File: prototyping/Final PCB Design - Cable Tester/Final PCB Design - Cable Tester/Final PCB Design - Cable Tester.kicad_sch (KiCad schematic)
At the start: 41 parts, among them J17 Banana Jack, J20 SFML-110-02-L-D-A, J3 Debug Connection, J4 MEM2061-01-188-00-A_REVA, J5 Barrel Jack 9V, J6 Touchscreen HMI, Q1 2N3904, SW1 Rocker Switch, U1 AVR128DB64x-xMR, U2 LP2985-3.3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

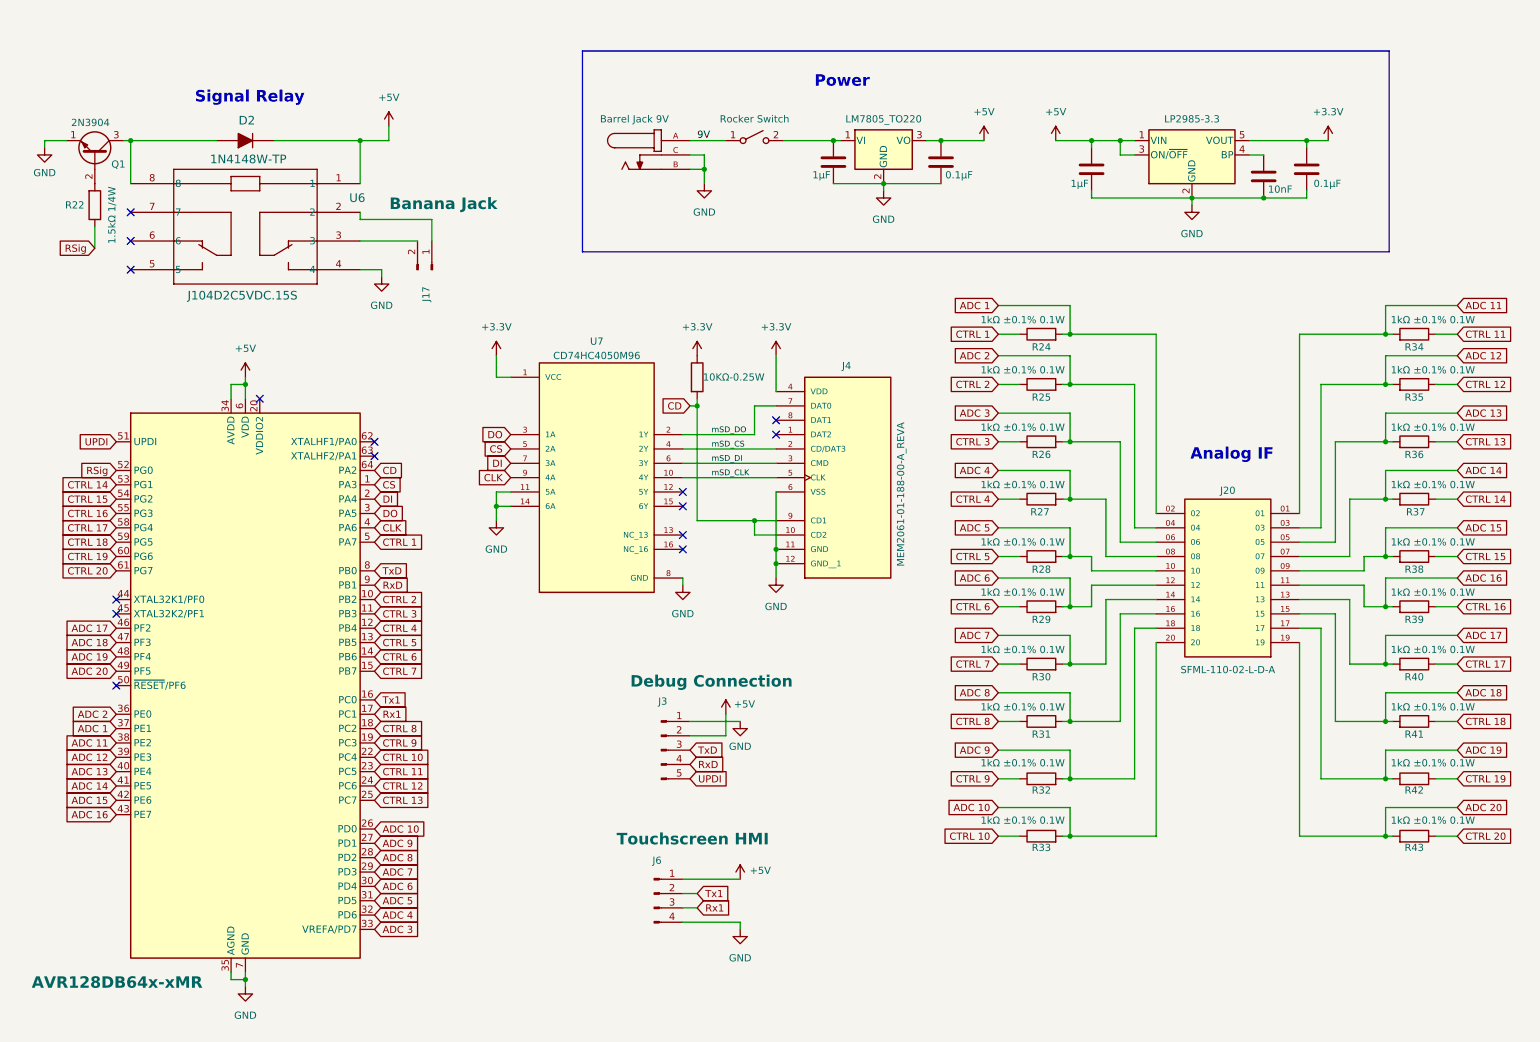
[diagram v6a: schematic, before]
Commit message: Update - Final PCB to JLCPCB components
Added the JLCPCB Library and updated to equivalent components supplied by JLCPCB. Also updated the PCB traces to fit new components.
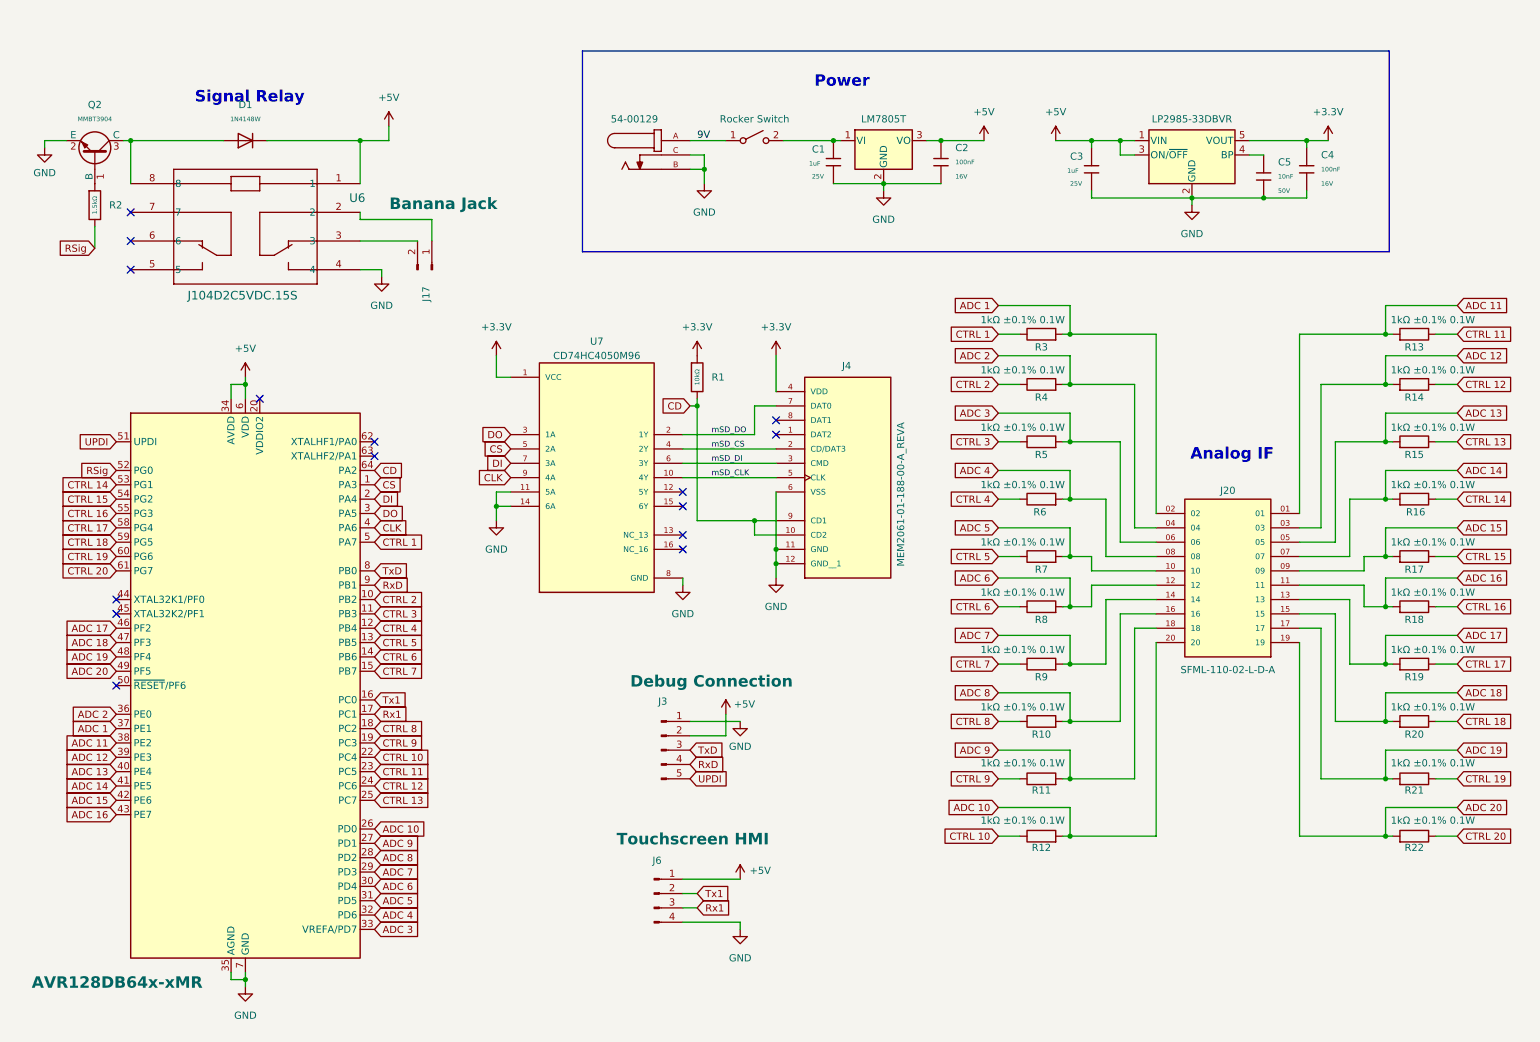
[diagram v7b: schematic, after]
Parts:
- removed C1, C3: 1µF, KiCad Symbols and Footprints:CAP_CL10_SAM, symbol Device:C
- removed C2, C4: 0.1µF, KiCad Symbols and Footprints:CAP_CL05_SAM, symbol Device:C
- removed C5: 10nF, KiCad Symbols and Footprints:CAPC10555_55N_KEM, symbol Device:C
- removed D2: 1N4148W-TP, digikey-footprints:SOD-123, symbol dk_Diodes-Rectifiers-Single:1N4148W-TP
- removed Q1: 2N3904, Package_TO_SOT_THT:TO-92_Inline, symbol Transistor_BJT:2N3904
- removed R2: 10KΩ-0.25W, KiCad Symbols and Footprints:RC0402N_PAN, symbol Device:R
- removed R22: 1.5kΩ 1/4W, KiCad Symbols and Footprints:RES_ERA8AEB152V, symbol Device:R
- added C1, C3: 1uF, PCM_JLCPCB:C_0402, symbol PCM_JLCPCB-Capacitors:0402,1uF
- added C2, C4: 100nF, PCM_JLCPCB:C_0402, symbol PCM_JLCPCB-Capacitors:0402,100nF
- added C5: 10nF, PCM_JLCPCB:C_0402, symbol PCM_JLCPCB-Capacitors:0402,10nF
- added D1: 1N4148W, PCM_JLCPCB:D_SOD-123, symbol PCM_JLCPCB-Diodes:Switching,1N4148W
- added Q2: MMBT3904, PCM_JLCPCB:Q_SOT-23, symbol PCM_JLCPCB-Transistors:NPN,MMBT3904
- added R1: 10kΩ, PCM_JLCPCB:R_1206, symbol PCM_JLCPCB-Resistors:1206,10kΩ
- added R2: 1.5kΩ, PCM_JLCPCB:R_0805, symbol PCM_JLCPCB-Resistors:0805,1.5kΩ
- J5: value Barrel Jack 9V -> 54-00129
- R10: renamed from R31; footprint KiCad Symbols and Footprints:RES_0816_SUS -> PCM_JLCPCB:R_0603
- R11: renamed from R32; footprint KiCad Symbols and Footprints:RES_0816_SUS -> PCM_JLCPCB:R_0603
- R12: renamed from R33; footprint KiCad Symbols and Footprints:RES_0816_SUS -> PCM_JLCPCB:R_0603
- R13: renamed from R34; footprint KiCad Symbols and Footprints:RES_0816_SUS -> PCM_JLCPCB:R_0603
- R14: renamed from R35; footprint KiCad Symbols and Footprints:RES_0816_SUS -> PCM_JLCPCB:R_0603
- R15: renamed from R36; footprint KiCad Symbols and Footprints:RES_0816_SUS -> PCM_JLCPCB:R_0603
- R16: renamed from R37; footprint KiCad Symbols and Footprints:RES_0816_SUS -> PCM_JLCPCB:R_0603
- R17: renamed from R38; footprint KiCad Symbols and Footprints:RES_0816_SUS -> PCM_JLCPCB:R_0603
- R18: renamed from R39; footprint KiCad Symbols and Footprints:RES_0816_SUS -> PCM_JLCPCB:R_0603
- R19: renamed from R40; footprint KiCad Symbols and Footprints:RES_0816_SUS -> PCM_JLCPCB:R_0603
- R20: renamed from R41; footprint KiCad Symbols and Footprints:RES_0816_SUS -> PCM_JLCPCB:R_0603
- R21: renamed from R42; footprint KiCad Symbols and Footprints:RES_0816_SUS -> PCM_JLCPCB:R_0603
- R22: renamed from R43; footprint KiCad Symbols and Footprints:RES_0816_SUS -> PCM_JLCPCB:R_0603
- R3: renamed from R24; footprint KiCad Symbols and Footprints:RES_0816_SUS -> PCM_JLCPCB:R_0603
- R4: renamed from R25; footprint KiCad Symbols and Footprints:RES_0816_SUS -> PCM_JLCPCB:R_0603
- R5: renamed from R26; footprint KiCad Symbols and Footprints:RES_0816_SUS -> PCM_JLCPCB:R_0603
- R6: renamed from R27; footprint KiCad Symbols and Footprints:RES_0816_SUS -> PCM_JLCPCB:R_0603
- R7: renamed from R28; footprint KiCad Symbols and Footprints:RES_0816_SUS -> PCM_JLCPCB:R_0603
- R8: renamed from R29; footprint KiCad Symbols and Footprints:RES_0816_SUS -> PCM_JLCPCB:R_0603
- R9: renamed from R30; footprint KiCad Symbols and Footprints:RES_0816_SUS -> PCM_JLCPCB:R_0603
- U2: value LP2985-3.3 -> LP2985-33DBVR
- U3: value LM7805_TO220 -> LM7805T
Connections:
- net +3.3V: now also C4.1, R1.1
- net +5V: now also C2.1, C3.1, D1.1
- net CD: now also R1.2
- net GND: now also C1.2, C2.2, C3.2, C4.2, C5.2, Q2.2 (E)
- net RSig: now also R2.2
- net at U2.4 (BP): now also C5.1
- net at U6.8: now also D1.2, Q2.3 (C)
- net at SW1.2 (B), U3.1 (VI): now also C1.1
- new net: Q2.1 (B), R2.1

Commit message: Update - Final PCB
Changed the Samtec connector and made minor adjustments
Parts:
- removed J20: SFML-110-02-L-D-A, KiCad Symbols and Footprints:SAMTEC_SFML-110-02-L-D-A, symbol SFML-110-02-L-D-A:SFML-110-02-L-D-A
- added J1: SFML-110-T1-S-D, KiCad Symbols and Footprints:SAMTEC_SFML-110-T1-S-D, symbol SFML-110-T1-S-D:SFML-110-T1-S-D
- SW1: value Rocker Switch -> 1x2 Pin header
- renumbered Q2 to Q1, U7 to U4
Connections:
- net ADC 1: now also J1.02
- net ADC 10: now also J1.20
- net ADC 11: now also J1.01
- net ADC 12: now also J1.03
- net ADC 13: now also J1.05
- net ADC 14: now also J1.07
- net ADC 15: now also J1.09
- net ADC 16: now also J1.11
- net ADC 17: now also J1.13
- net ADC 18: now also J1.15
- net ADC 19: now also J1.17
- net ADC 2: now also J1.04
- net ADC 20: now also J1.19
- net ADC 3: now also J1.06
- net ADC 4: now also J1.08
- net ADC 5: now also J1.10
- net ADC 6: now also J1.12
- net ADC 7: now also J1.14
- net ADC 8: now also J1.16
- net ADC 9: now also J1.18
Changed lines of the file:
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@@
 					(size 1.27 1.27)
 				)
-				(hide yes)
 			)
 		)
@@
 					(size 1.27 1.27)
 				)
-				(hide yes)
 			)
 		)
@@
 		(on_board yes)
 		(dnp no)
-		(property "Reference" "U7"
+		(property "Reference" "U4"
 			(at 119.38 72.39 0)
 			(effects
@@
 			(project ""
 				(path "/9839a162-8d53-4cc7-8474-cf7807328c6e"
-					(reference "U7")
+					(reference "U4")
 					(unit 1)
 				)
@@
 				)
 				(justify left)
-				(hide yes)
 			)
 		)
@@
 	)
 	(symbol
-		(lib_id "SFML-110-02-L-D-A:SFML-110-02-L-D-A")
-		(at 231.14 113.03 0)
-		(mirror y)
-		(unit 1)
-		(exclude_from_sim no)
-		(in_bom yes)
-		(on_board yes)
-		(dnp no)
-		(property "Reference" "J20"
-			(at 231.14 98.806 0)
-			(effects
-				(font
-					(size 1.27 1.27)
-				)
-			)
-		)
-		(property "Value" "SFML-110-02-L-D-A"
-			(at 231.14 130.556 0)
-			(effects
-				(font
-					(size 1.27 1.27)
-				)
-			)
-		)
-		(property "Footprint" "KiCad Symbols and Footprints:SAMTEC_SFML-110-02-L-D-A"
-			(at 231.14 113.03 0)
-			(effects
-				(font
-					(size 1.27 1.27)
-				)
-				(justify bottom)
-				(hide yes)
-			)
-		)
-		(property "Datasheet" ""
-			(at 231.14 113.03 0)
-			(effects
-				(font
-					(size 1.27 1.27)
-				)
-				(hide yes)
-			)
-		)
-		(property "Description" "JLCPCB Part # C5910777"
-			(at 231.14 113.03 0)
-			(effects
-				(font
-					(size 1.27 1.27)
-				)
-				(hide yes)
-			)
-		)
-		(property "PARTREV" "E"
-			(at 231.14 113.03 0)
-			(effects
-				(font
-					(size 1.27 1.27)
-				)
-				(justify bottom)
-				(hide yes)
-			)
-		)
-		(property "STANDARD" "Manufacturer Recommendations"
-			(at 231.14 113.03 0)
-			(effects
-				(font
-					(size 1.27 1.27)
-				)
-				(justify bottom)
-				(hide yes)
-			)
-		)
-		(property "MANUFACTURER" "SAMTEC"
-			(at 231.14 113.03 0)
-			(effects
-				(font
-					(size 1.27 1.27)
-				)
-				(justify bottom)
-				(hide yes)
-			)
-		)
-		(pin "20"
-		)
-		(pin "08"
-		)
-		(pin "09"
-		)
-		(pin "11"
-		)
-		(pin "06"
-		)
-		(pin "14"
-		)
-		(pin "12"
-		)
-		(pin "04"
-		)
-		(pin "15"
-		)
-		(pin "18"
-		)
-		(pin "02"
-		)
-		(pin "03"
-		)
-		(pin "19"
-		)
-		(pin "05"
-		)
-		(pin "01"
-		)
-		(pin "07"
-		)
-		(pin "17"
-		)
-		(pin "13"
-		)
-		(pin "16"
-		)
-		(pin "10"
-		)
-		(instances
-			(project "Final PCB Design - Cable Tester"
-				(path "/9839a162-8d53-4cc7-8474-cf7807328c6e"
-					(reference "J20")
-					(unit 1)
-				)
-			)
-		)
-	)
-	(symbol
 		(lib_id "PCM_JLCPCB-Capacitors:0402,100nF")
 		(at 180.34 40.64 0)
@@
 					(size 1.27 1.27)
 				)
-				(hide yes)
 			)
 		)
@@
 					(size 1.27 1.27)
 				)
-				(hide yes)
 			)
 		)
-		(property "Value" "Rocker Switch"
+		(property "Value" "1x2 Pin header"
 			(at 147.32 33.02 0)
 			(effects
@@
 			)
 		)
-		(property "Description" "Single Pole Single Throw (SPST) switch, separate symbol"
+		(property "Description" "Header to connect to the box switch"
 			(at 147.32 36.83 0)
 			(effects
@@
 		(dnp no)
 		(property "Reference" "U6"
-			(at 76.962 46.99 0)
+			(at 57.15 67.31 0)
 			(effects
 				(font
@@
 		(on_board yes)
 		(dnp no)
-		(fields_autoplaced yes)
 		(property "Reference" "D1"
-			(at 57.15 30.48 90)
+			(at 57.15 39.878 90)
 			(effects
 				(font
@@
 	)
 	(symbol
+		(lib_id "SFML-110-T1-S-D:SFML-110-T1-S-D")
+		(at 231.14 113.03 0)
+		(mirror y)
+		(unit 1)
+		(exclude_from_sim no)
+		(in_bom yes)
+		(on_board yes)
+		(dnp no)
+		(property "Reference" "J1"
+			(at 231.14 95.25 0)
+			(effects
+				(font
+					(size 1.27 1.27)
+				)
+			)
+		)
+		(property "Value" "SFML-110-T1-S-D"
+			(at 231.14 97.79 0)
+			(effects
+				(font
+					(size 1.27 1.27)
+				)
+			)
+		)
+		(property "Footprint" "KiCad Symbols and Footprints:SAMTEC_SFML-110-T1-S-D"
+			(at 231.14 113.03 0)
+			(effects
+				(font
+					(size 1.27 1.27)
+				)
+				(justify bottom)
+				(hide yes)
+			)
+		)
+		(property "Datasheet" ""
+			(at 231.14 113.03 0)
+			(effects
+				(font
+					(size 1.27 1.27)
+				)
+				(hide yes)
+			)
+		)
+		(property "Description" "Digikey Part # SAM8241-ND / JLCPCB Part # C5886728"
+			(at 231.14 113.03 0)
+			(effects
+				(font
+					(size 1.27 1.27)
+				)
+				(hide yes)
+			)
+		)
+		(property "PARTREV" "E"
+			(at 231.14 113.03 0)
+			(effects
+				(font
+					(size 1.27 1.27)
+				)
+				(justify bottom)
+				(hide yes)
+			)
+		)
+		(property "STANDARD" "Manufacturer Recommendations"
+			(at 231.14 113.03 0)
+			(effects
+				(font
+					(size 1.27 1.27)
+				)
+				(justify bottom)
+				(hide yes)
+			)
+		)
+		(property "MANUFACTURER" "SAMTEC"
+			(at 231.14 113.03 0)
+			(effects
+				(font
+					(size 1.27 1.27)
+				)
+				(justify bottom)
+				(hide yes)
+			)
+		)
+		(pin "06"
+		)
+		(pin "12"
+		)
+		(pin "13"
+		)
+		(pin "03"
+		)
+		(pin "11"
+		)
+		(pin "17"
+		)
+		(pin "02"
+		)
+		(pin "05"
+		)
+		(pin "07"
+		)
+		(pin "09"
+		)
+		(pin "15"
+		)
+		(pin "19"
+		)
+		(pin "04"
+		)
+		(pin "08"
+		)
+		(pin "01"
+		)
+		(pin "10"
+		)
+		(pin "14"
+		)
+		(pin "16"
+		)
+		(pin "18"
+		)
+		(pin "20"
+		)
+		(instances
+			(project ""
+				(path "/9839a162-8d53-4cc7-8474-cf7807328c6e"
+					(reference "J1")
+					(unit 1)
+				)
+			)
+		)
+	)
+	(symbol
 		(lib_id "Device:R")
 		(at 198.12 149.86 90)
@@
 		(dnp no)
 		(fields_autoplaced yes)
-		(property "Reference" "Q2"
+		(property "Reference" "Q1"
 			(at 30.48 30.48 90)
 			(effects
@@
 			(project ""
 				(path "/9839a162-8d53-4cc7-8474-cf7807328c6e"
-					(reference "Q2")
+					(reference "Q1")
 					(unit 1)
 				)
